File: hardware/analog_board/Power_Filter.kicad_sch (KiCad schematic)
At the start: 93 parts, among them U9 TPS54360DDA

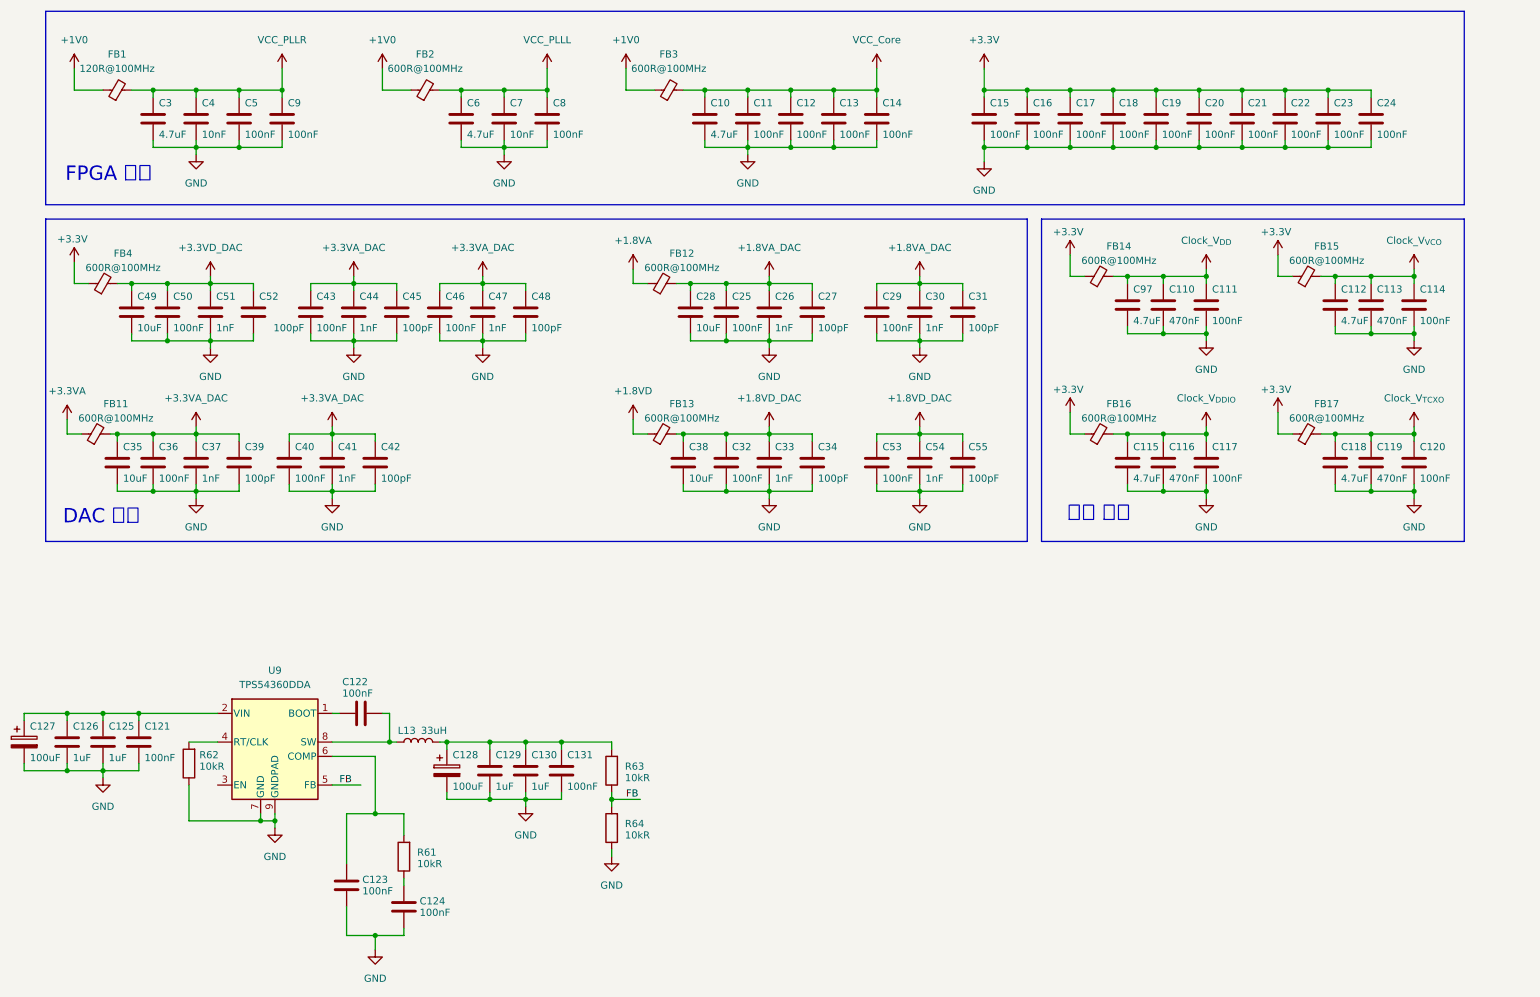
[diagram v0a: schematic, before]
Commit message: feat：模拟板电源 原理图设计
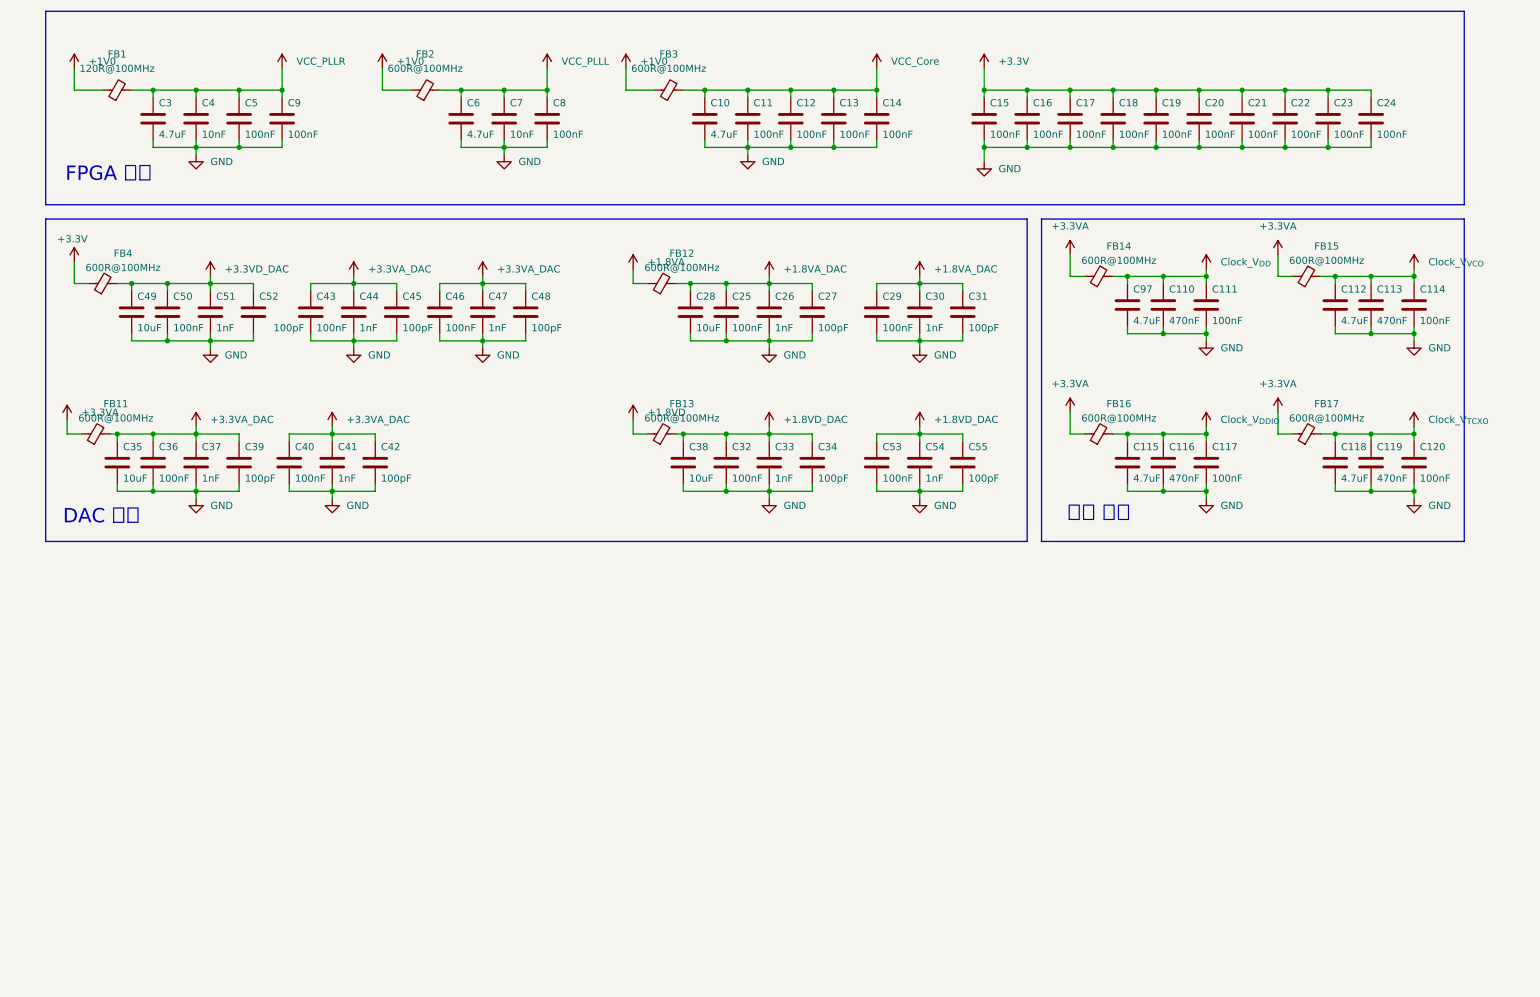
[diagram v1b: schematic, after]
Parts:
- removed C121, C122, C123, C124, C131: 100nF, Capacitor_SMD:C_0603_1608Metric, symbol Device:C
- removed C125, C126, C129, C130: 1uF, Capacitor_SMD:C_1206_3216Metric, symbol Device:C
- removed C127, C128: 100uF, symbol Device:C_Polarized
- removed L13: 33uH, symbol Device:L
- removed R61, R62, R63, R64: 10kR, Resistor_SMD:R_0603_1608Metric, symbol Device:R
- removed U9: TPS54360DDA, Package_SO:TI_SO-PowerPAD-8_ThermalVias, symbol Regulator_Switching:TPS54360DDA
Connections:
- net +3.3V: no longer FB14.1, FB15.1, FB16.1, FB17.1
- net +3.3VA: now also FB14.1, FB15.1, FB16.1, FB17.1

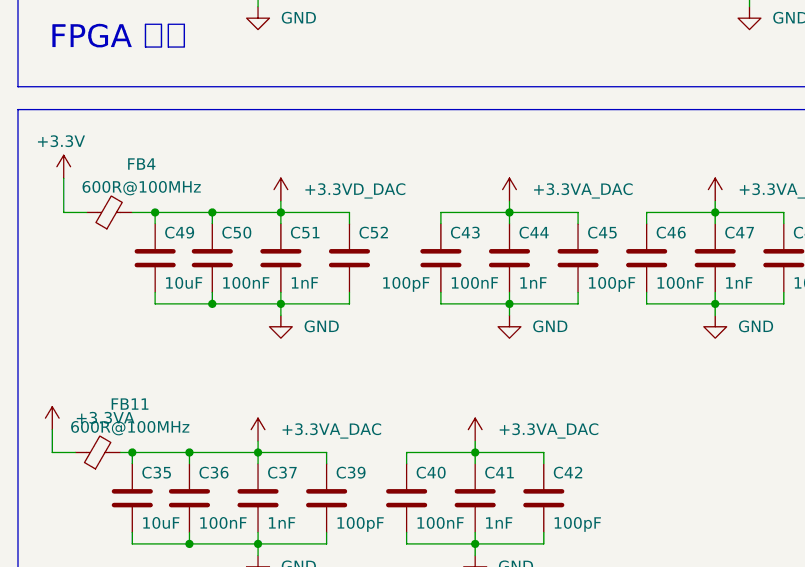
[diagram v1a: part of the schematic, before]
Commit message: feat：根据PCB微调原理图
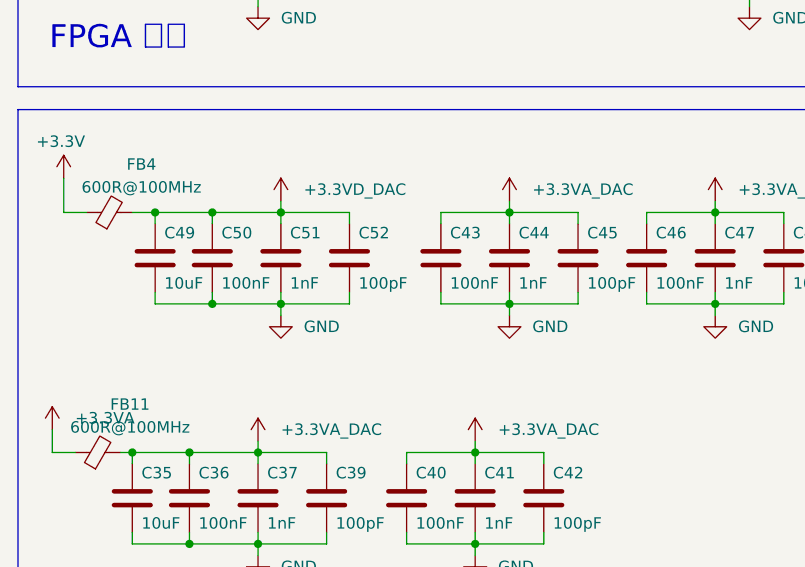
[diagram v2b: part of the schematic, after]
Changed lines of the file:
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@@
 		)
 		(property "Value" "100pF"
-			(at 61.976 77.724 0)
+			(at 59.436 77.724 0)
 			(show_name no)
 			(do_not_autoplace no)
